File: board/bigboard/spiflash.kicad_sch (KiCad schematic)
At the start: 4 parts, among them J11 Conn_01x02_Male, U7 GD25LQ128DSIGR

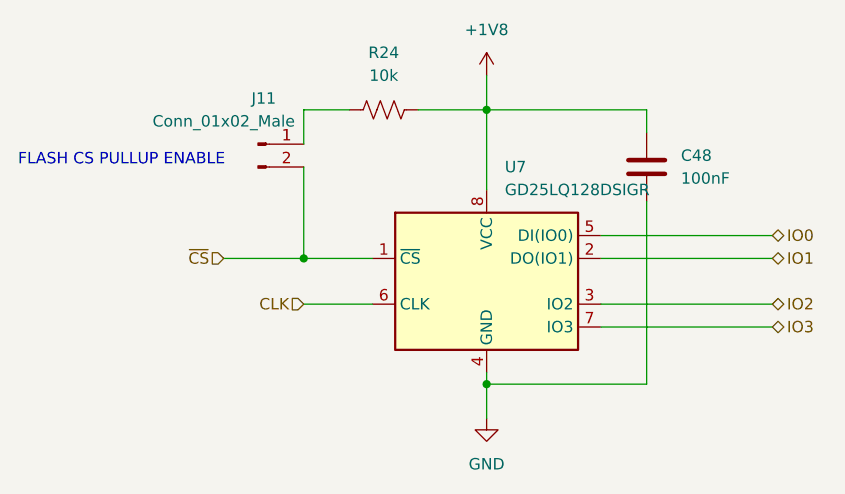
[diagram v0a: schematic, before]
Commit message: Manufactured version of bigboard
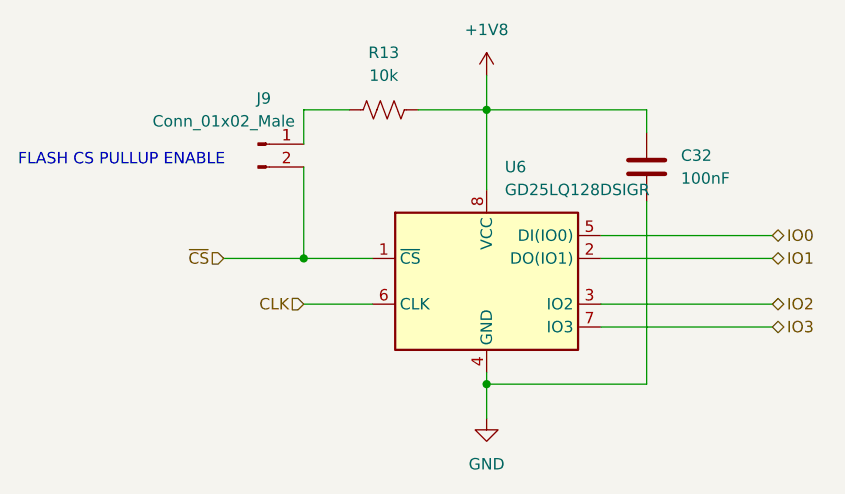
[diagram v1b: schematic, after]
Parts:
- C32: renamed from C48; MPN (none) -> CC0201KRX5R8BB104
- R13: renamed from R24; MPN (none) -> RC0201FR-0710KL
- renumbered J11 to J9, U7 to U6
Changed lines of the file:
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@@
   (symbol (lib_id "Memory_Flash:W25Q128JVS") (at 152.4 102.87 0) (unit 1)
     (in_bom yes) (on_board yes) (fields_autoplaced)
-    (property "Reference" "U7" (id 0) (at 154.4194 90.17 0)
+    (property "Reference" "U6" (id 0) (at 154.4194 90.17 0)
       (effects (font (size 1.27 1.27)) (justify left))
     )
@@
   (symbol (lib_id "power:GND") (at 152.4 118.11 0) (unit 1)
     (in_bom yes) (on_board yes) (fields_autoplaced)
-    (property "Reference" "#PWR038" (id 0) (at 152.4 124.46 0)
+    (property "Reference" "#PWR034" (id 0) (at 152.4 124.46 0)
       (effects (font (size 1.27 1.27)) hide)
     )
@@
   (symbol (lib_id "Connector:Conn_01x02_Male") (at 127 87.63 0) (unit 1)
     (in_bom yes) (on_board yes)
-    (property "Reference" "J11" (id 0) (at 127.635 82.55 0))
+    (property "Reference" "J9" (id 0) (at 127.635 82.55 0))
     (property "Value" "Conn_01x02_Male" (id 1) (at 123.19 85.09 0))
     (property "Footprint" "Connector_PinHeader_2.54mm:PinHeader_1x02_P2.54mm_Vertical" (id 2) (at 127 87.63 0)
@@
   (symbol (lib_id "Device:R_US") (at 140.97 83.82 90) (unit 1)
     (in_bom yes) (on_board yes) (fields_autoplaced)
-    (property "Reference" "R24" (id 0) (at 140.97 77.47 90))
+    (property "Reference" "R13" (id 0) (at 140.97 77.47 90))
     (property "Value" "10k" (id 1) (at 140.97 80.01 90))
     (property "Footprint" "Resistor_SMD:R_0201_0603Metric" (id 2) (at 141.224 82.804 90)
@@
       (effects (font (size 1.27 1.27)) hide)
     )
+    (property "MPN" "RC0201FR-0710KL" (id 5) (at 140.97 83.82 0)
+      (effects (font (size 1.27 1.27)) hide)
+    )
     (pin "1")
     (pin "2")
@@
   (symbol (lib_id "power:+1V8") (at 152.4 80.01 0) (unit 1)
     (in_bom yes) (on_board yes) (fields_autoplaced)
-    (property "Reference" "#PWR037" (id 0) (at 152.4 83.82 0)
+    (property "Reference" "#PWR033" (id 0) (at 152.4 83.82 0)
       (effects (font (size 1.27 1.27)) hide)
     )
@@
   (symbol (lib_id "Device:C") (at 170.18 90.17 0) (unit 1)
     (in_bom yes) (on_board yes) (fields_autoplaced)
-    (property "Reference" "C48" (id 0) (at 173.99 88.8999 0)
+    (property "Reference" "C32" (id 0) (at 173.99 88.8999 0)
       (effects (font (size 1.27 1.27)) (justify left))
     )
@@
       (effects (font (size 1.27 1.27)) hide)
     )
+    (property "MPN" "CC0201KRX5R8BB104" (id 5) (at 170.18 90.17 0)
+      (effects (font (size 1.27 1.27)) hide)
+    )
